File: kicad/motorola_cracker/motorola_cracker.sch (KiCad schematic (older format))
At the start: 27 parts, among them J1 DB9, P1 CONN_6, P2 CONN_2, U1 78L10, U2 74LS245, U3 MAX232, U4 78L05, U5 68HC11_PLCC, X1 4Mhz

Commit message: motorola_cracker update
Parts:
- removed C7: 100n, symbol C
- added P3: CONN_6, symbol CONN_6
- U5: value 68HC11_PLCC -> 68HC05_PLCC
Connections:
- net labels added: TX
- wire segments 98 -> 107
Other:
- moved on the sheet: C2, C3, C9, P1, R2, R7, R8, R9, U5, X1

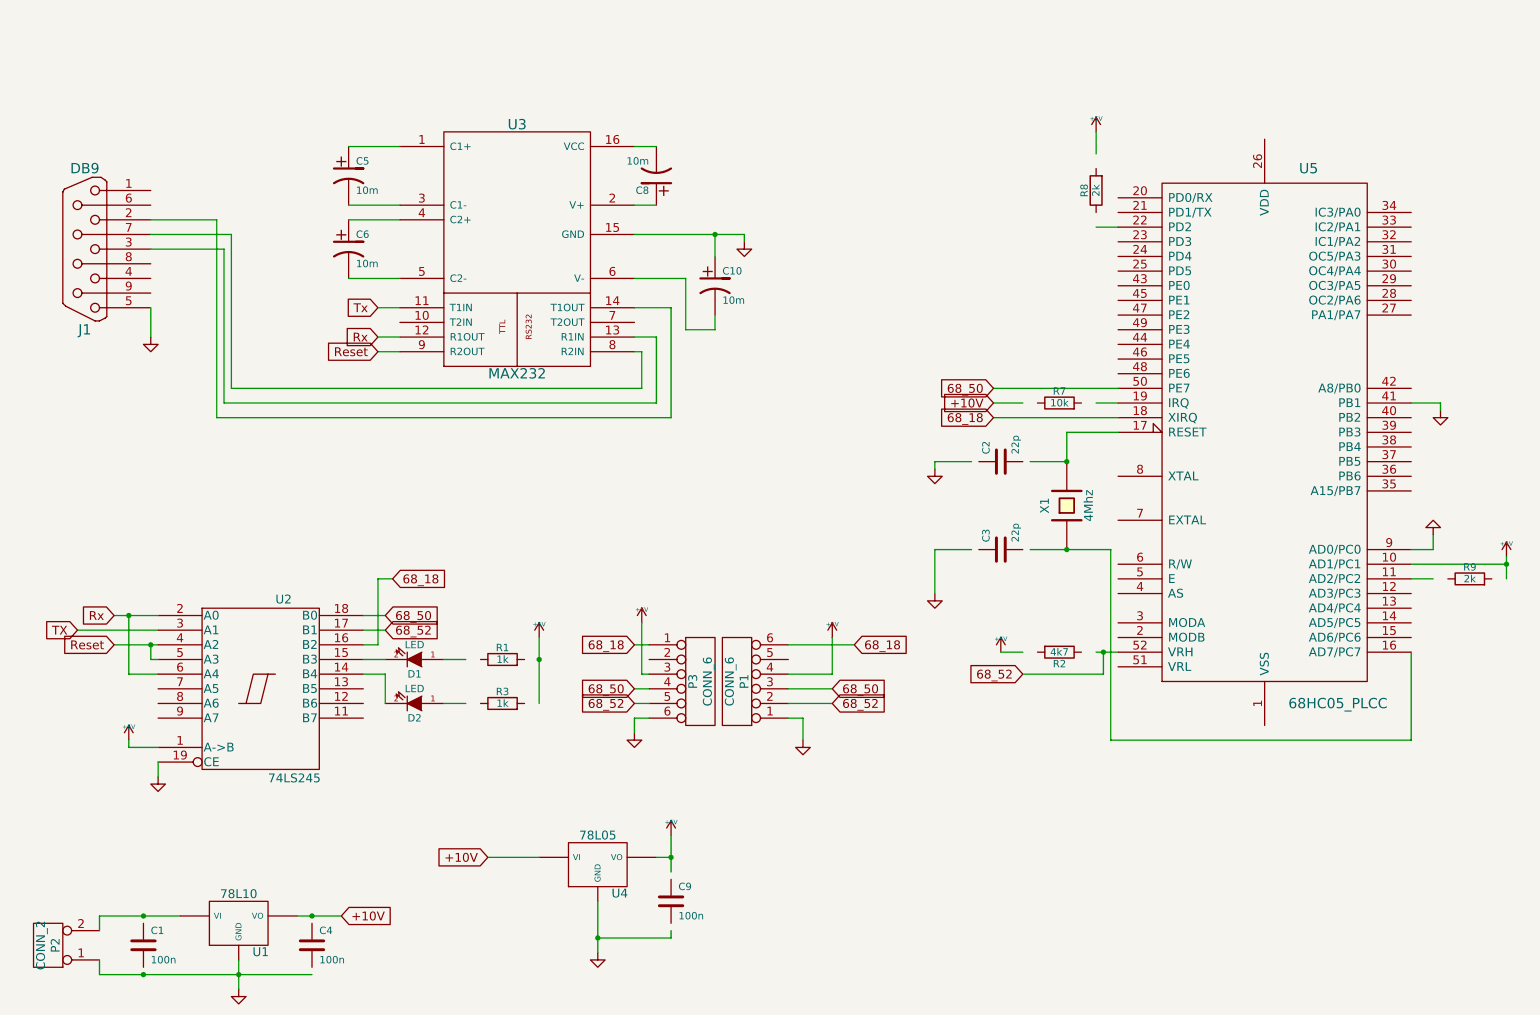
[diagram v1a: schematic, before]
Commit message: update cpu board to fit 50x50cm for dirtypcb servis req.
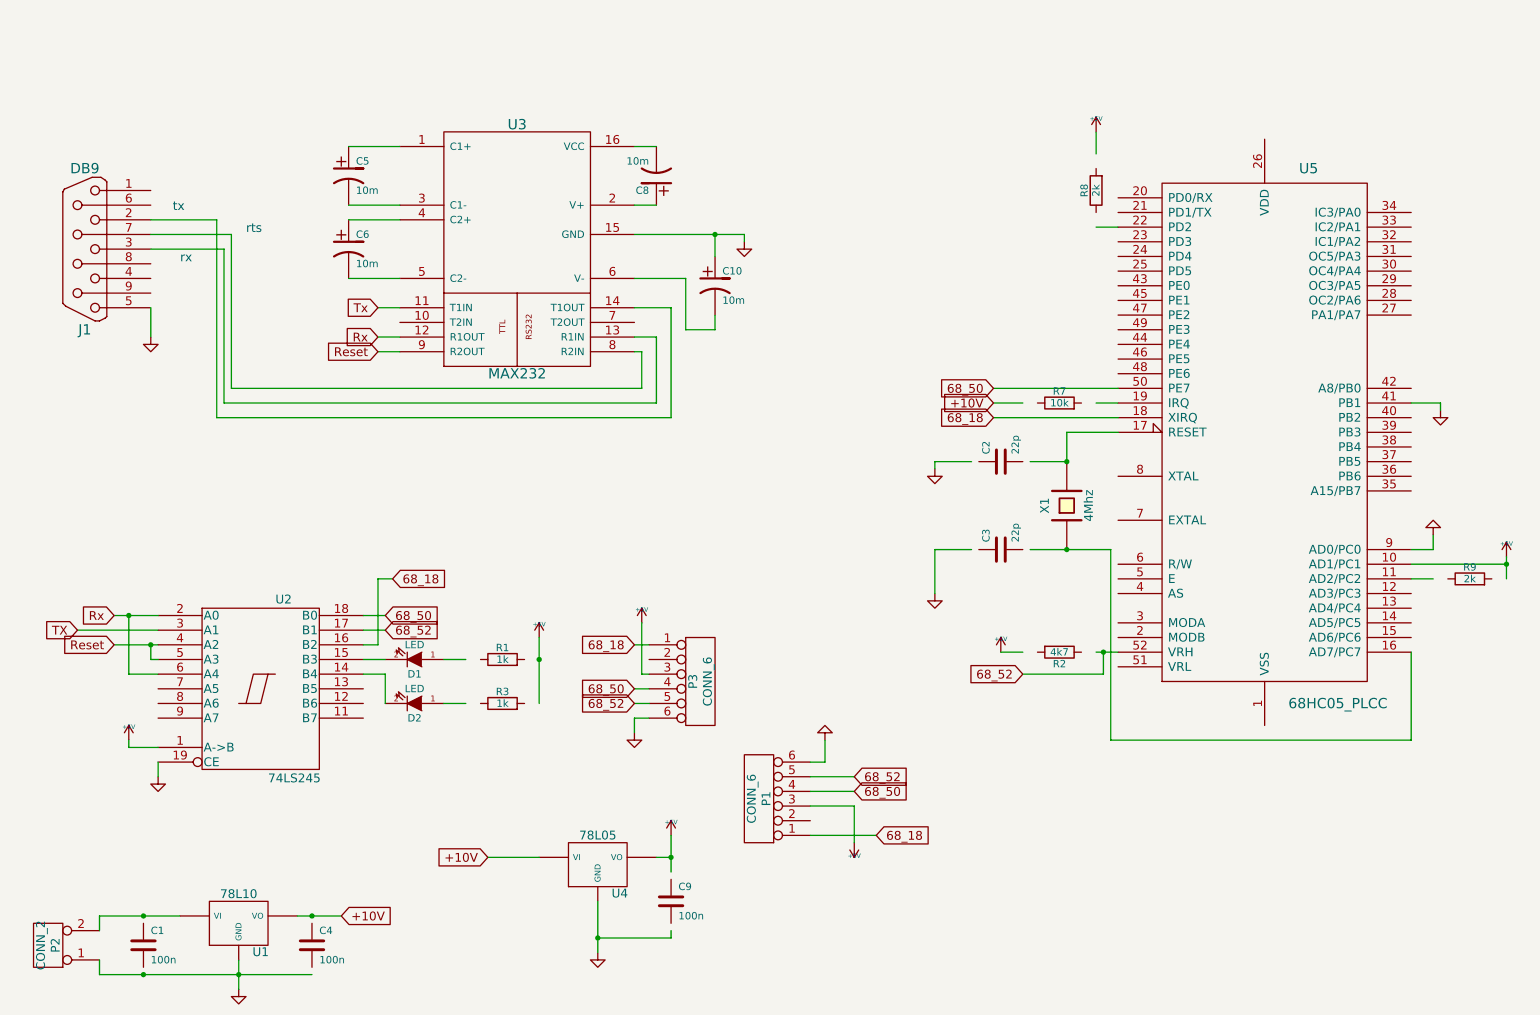
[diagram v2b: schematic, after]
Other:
- note added: "rts"
- note added: "rx"
- note added: "tx"
- moved on the sheet: P1
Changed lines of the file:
@@
 	1    0    0    -1
 $EndComp
-Text GLabel 6200 5550 2    60   Input ~ 0
+Text GLabel 6350 6050 2    60   Input ~ 0
 68_52
-Text GLabel 6350 5150 2    60   Input ~ 0
+Text GLabel 6500 6450 2    60   Input ~ 0
 68_18
-Text GLabel 6200 5450 2    60   Input ~ 0
+Text GLabel 6350 6150 2    60   Input ~ 0
 68_50
 Text GLabel 7500 5350 0    60   Input ~ 0
@@
 L GND #PWR011
 U 1 1 52DBC8C7
-P 6000 5800
-F 0 "#PWR011" H 6000 5800 30  0001 C CNN
-F 1 "GND" H 6000 5730 30  0001 C CNN
-F 2 "" H 6000 5800 60  0001 C CNN
-F 3 "" H 6000 5800 60  0001 C CNN
-	1    6000 5800
-	1    0    0    -1
+P 6150 5800
+F 0 "#PWR011" H 6150 5800 30  0001 C CNN
+F 1 "GND" H 6150 5730 30  0001 C CNN
+F 2 "" H 6150 5800 60  0001 C CNN
+F 3 "" H 6150 5800 60  0001 C CNN
+	1    6150 5800
+	-1   0    0    1
 $EndComp
 $Comp
 L CONN_6 P1
 U 1 1 52DBC7F5
-P 5550 5400
-F 0 "P1" V 5500 5400 60  0000 C CNN
-F 1 "CONN_6" V 5600 5400 60  0000 C CNN
-F 2 "" H 5550 5400 60  0001 C CNN
-F 3 "" H 5550 5400 60  0001 C CNN
-	1    5550 5400
+P 5700 6200
+F 0 "P1" V 5650 6200 60  0000 C CNN
+F 1 "CONN_6" V 5750 6200 60  0000 C CNN
+F 2 "" H 5700 6200 60  0001 C CNN
+F 3 "" H 5700 6200 60  0001 C CNN
+	1    5700 6200
 	-1   0    0    1
 $EndComp
@@
 L +5V #PWR016
 U 1 1 52DAF45F
-P 6200 5100
-F 0 "#PWR016" H 6200 5190 20  0001 C CNN
-F 1 "+5V" H 6200 5190 30  0000 C CNN
-F 2 "" H 6200 5100 60  0001 C CNN
-F 3 "" H 6200 5100 60  0001 C CNN
-	1    6200 5100
-	1    0    0    -1
+P 6350 6500
+F 0 "#PWR016" H 6350 6590 20  0001 C CNN
+F 1 "+5V" H 6350 6590 30  0000 C CNN
+F 2 "" H 6350 6500 60  0001 C CNN
+F 3 "" H 6350 6500 60  0001 C CNN
+	1    6350 6500
+	-1   0    0    1
 $EndComp
 $Comp
@@
 	4850 1750 5000 1750
 Wire Wire Line
-	5900 5150 6350 5150
-Wire Wire Line
-	6200 5550 5900 5550
+	6050 6450 6500 6450
+Wire Wire Line
+	6350 6050 6050 6050
 Wire Wire Line
 	7300 3600 8150 3600
@@
 	1200 7400 1200 7300
 Wire Wire Line
-	6200 5100 6200 5350
-Wire Wire Line
-	6200 5350 5900 5350
+	6350 6250 6350 6500
+Wire Wire Line
+	6350 6250 6050 6250
 Wire Wire Line
 	8000 2300 8150 2300
@@
 	8150 3500 8000 3500
 Wire Wire Line
-	6000 5800 6000 5650
-Wire Wire Line
-	6000 5650 5900 5650
+	6150 5950 6150 5800
+Wire Wire Line
+	6150 5950 6050 5950
 Wire Wire Line
 	1750 7000 1200 7000
@@
 Connection ~ 8050 5200
 Wire Wire Line
-	6200 5450 5900 5450
+	6350 6150 6050 6150
 Wire Wire Line
 	1600 6050 1600 5950
@@
 Wire Wire Line
 	5100 7150 4600 7150
+Text Notes 1700 2200 0    60   ~ 0
+tx
+Text Notes 1750 2550 0    60   ~ 0
+rx
+Text Notes 2200 2350 0    60   ~ 0
+rts
 $EndSCHEMATC

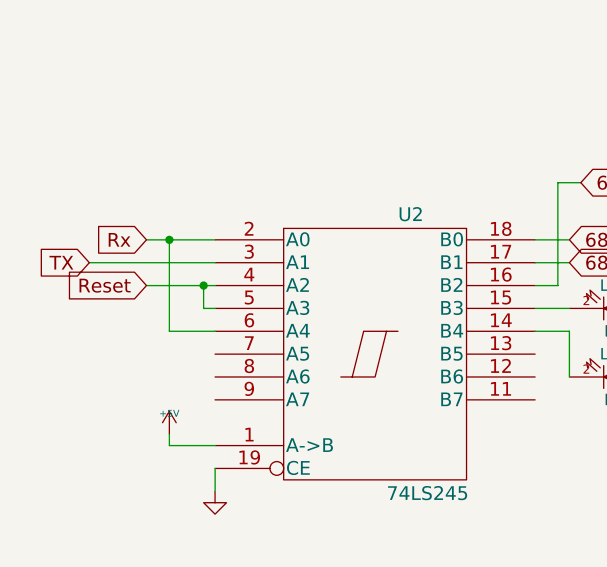
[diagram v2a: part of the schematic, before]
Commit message: remke pcb's to match 5x5cm
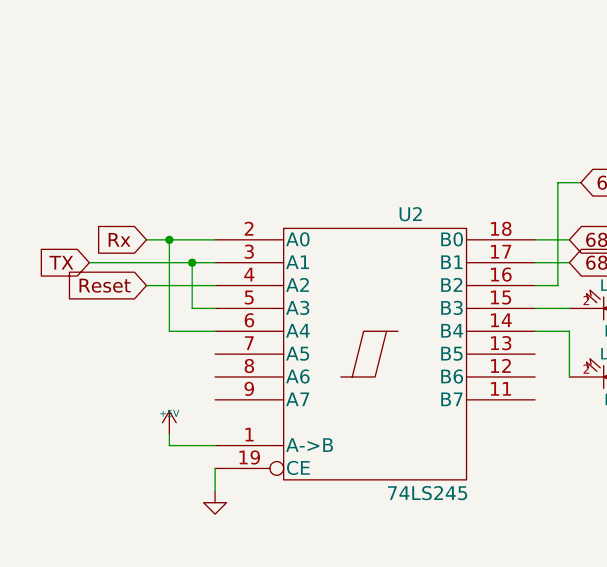
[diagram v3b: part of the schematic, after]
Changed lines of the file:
@@
 Wire Wire Line
 	1300 5150 1600 5150
-Connection ~ 1550 5150
 Wire Wire Line
 	1050 5050 1600 5050
@@
 Connection ~ 4600 7150
 Wire Wire Line
-	1550 5150 1550 5250
-Wire Wire Line
-	1550 5250 1600 5250
+	1500 5250 1600 5250
 Wire Wire Line
 	3250 3050 3100 3050
@@
 Text Notes 2200 2350 0    60   ~ 0
 rts
+Wire Wire Line
+	1500 5250 1500 5050
+Connection ~ 1500 5050
 $EndSCHEMATC

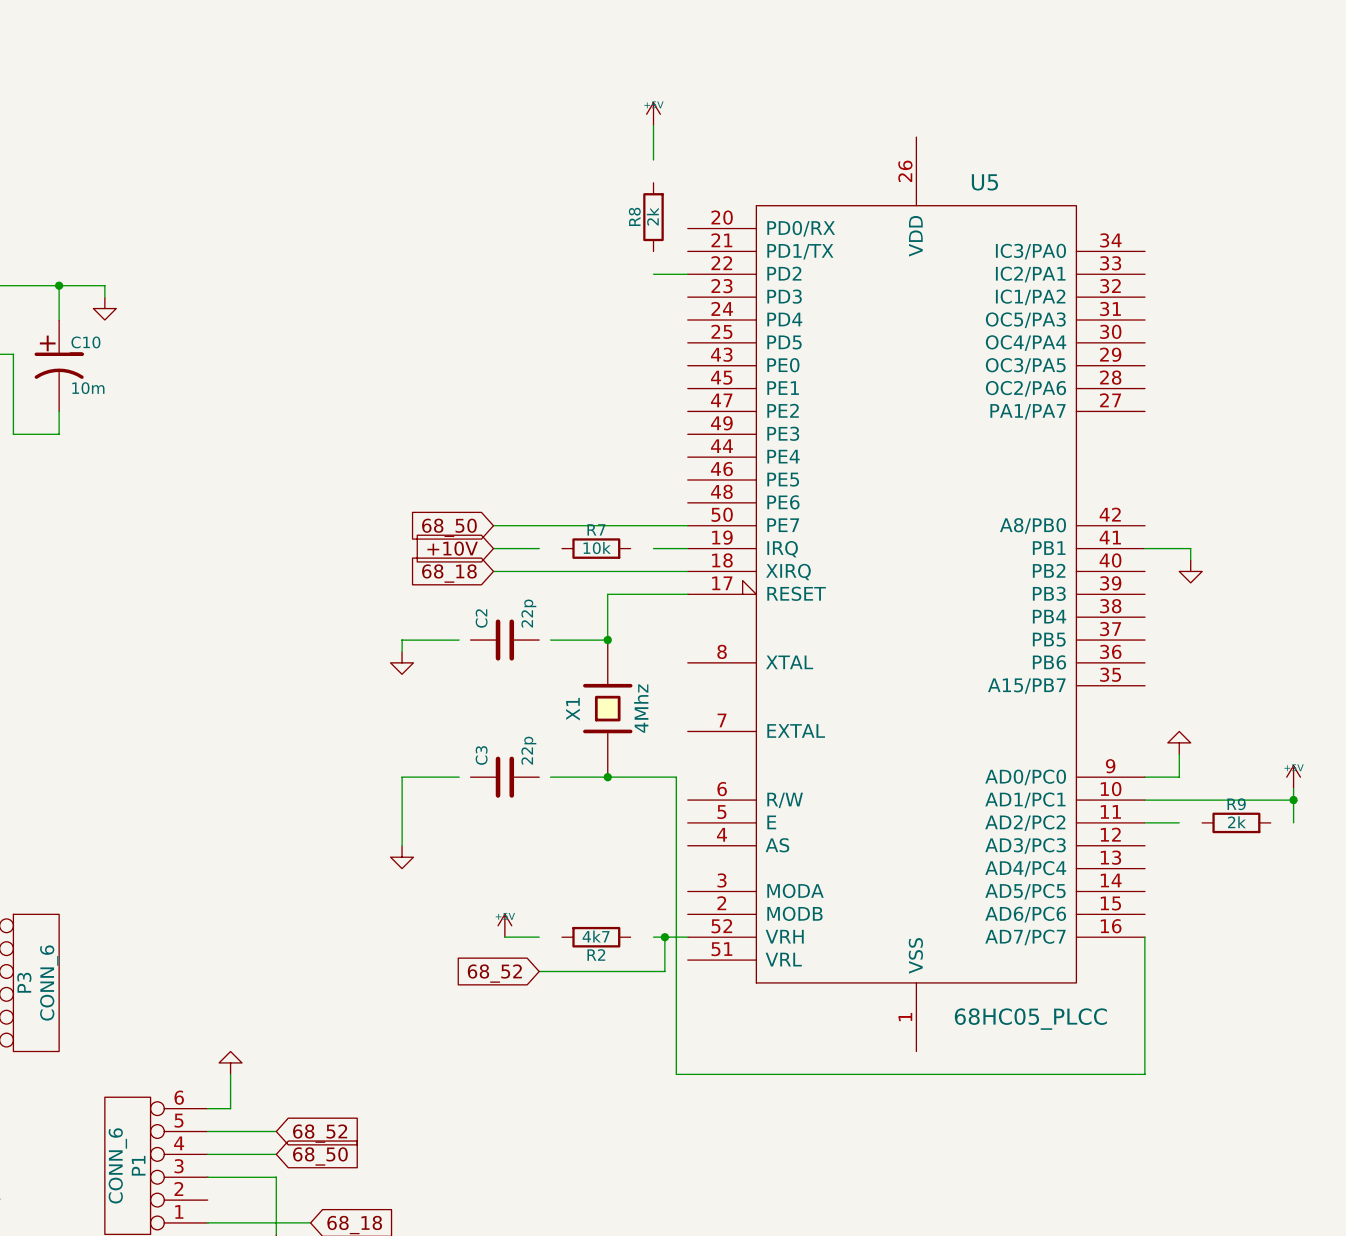
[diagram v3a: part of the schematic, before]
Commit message: added switch to select 68HC05/68HC705 based on schematics mc68hc05-705.JPG
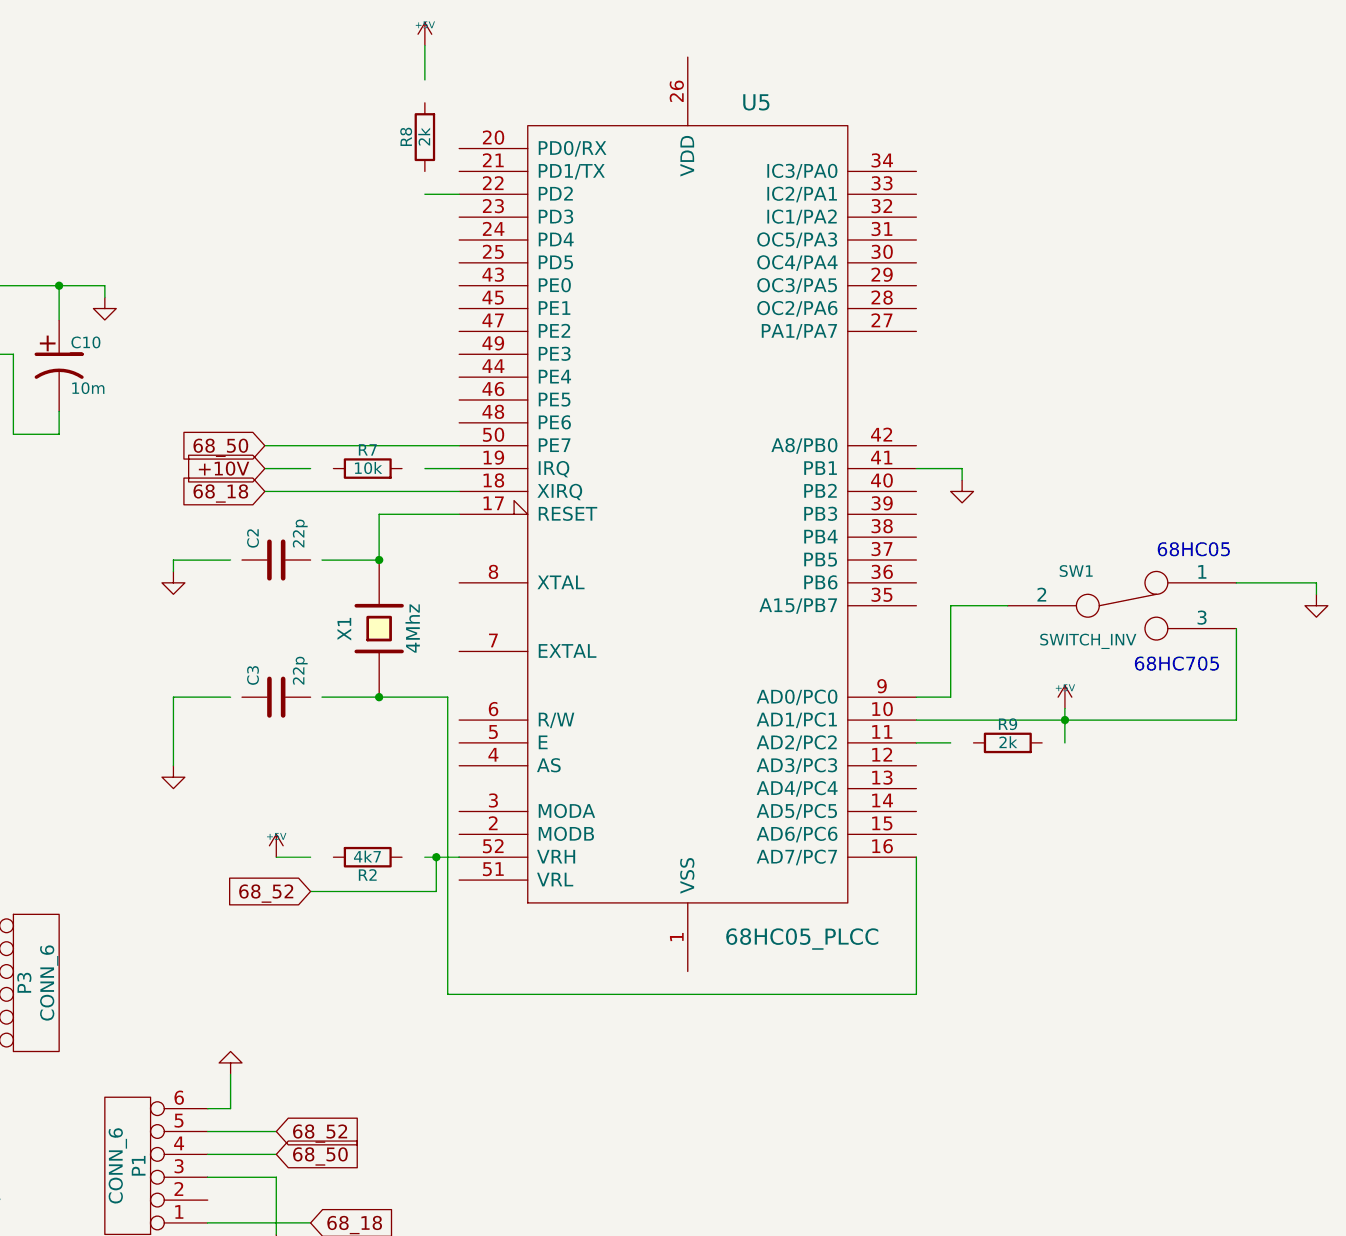
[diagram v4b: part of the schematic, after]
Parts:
- added SW1: SWITCH_INV, Pin_Headers:Pin_Header_Straight_1x03, symbol SWITCH_INV
- C1, C4, C9: footprint (none) -> Capacitors_ThroughHole:Capacitor3MMDiscRM2.5
- C10, C5, C6, C8: footprint (none) -> Capacitors_Elko_ThroughHole:Elko_vert_DM10_RM5
- C2, C3: footprint (none) -> Capacitors_ThroughHole:Capacitor6MMDiscRM5
- D1, D2: footprint (none) -> LEDs:LED-5MM
- J1: footprint (none) -> Connect:DB9FC
- P1: footprint (none) -> Socket_Strips:Socket_Strip_Angled_1x06
- P2: footprint (none) -> Connect:AK300-2
- P3: footprint (none) -> Pin_Headers:Pin_Header_Angled_1x06
- R1, R2, R3, R7, R8, R9: footprint (none) -> Resistors_ThroughHole:Resistor_Horizontal_RM10mm
- U1, U4: footprint (none) -> my_modules:TO92-STABIL
- U2: footprint (none) -> Sockets_DIP:DIP-20__300_ELL
- U3: footprint (none) -> Sockets_DIP:DIP-16__300_ELL
- U5: footprint (none) -> Sockets:PLCC52
- X1: footprint (none) -> Crystals:Crystal_HC49-U_Vertical
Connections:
- wire segments 107 -> 111
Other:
- note added: "68HC05"
- note added: "68HC705"
- moved on the sheet: C2, C3, R2, R7, R8, R9, U5, X1

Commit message: motorola cracker simple board for usb to serial dongle (tested with cp2102)
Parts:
- removed C10, C5, C6, C8: 10m, Capacitors_Elko_ThroughHole:Elko_vert_DM10_RM5, symbol CP1
- removed D1, D2: LED, LEDs:LED-5MM, symbol LED
- removed J1: DB9, Connect:DB9FC, symbol DB9
- removed P3: CONN_6, Pin_Headers:Pin_Header_Angled_1x06, symbol CONN_6
- removed R1, R3: 1k, Resistors_ThroughHole:Resistor_Horizontal_RM10mm, symbol R
- removed R2: 4k7, Resistors_ThroughHole:Resistor_Horizontal_RM10mm, symbol R
- removed SW1: SWITCH_INV, Pin_Headers:Pin_Header_Straight_1x03, symbol SWITCH_INV
- removed U2: 74LS245, Sockets_DIP:DIP-20__300_ELL, symbol 74LS245
- removed U3: MAX232, Sockets_DIP:DIP-16__300_ELL, symbol MAX232
- removed U5: 68HC05_PLCC, Sockets:PLCC52, symbol 68HC11_PLCC
- added C5: 100n, Capacitors_ThroughHole:C_Disc_D3_P2.5, symbol C
- added JP1: JUMPER3, Pin_Headers:Pin_Header_Straight_1x03, symbol JUMPER3
- added P3: CONN_5, Pin_Headers:Pin_Header_Straight_1x01, symbol CONN_01X01
- added R1: 10k, Resistors_ThroughHole:Resistor_Horizontal_RM10mm, symbol R-RESCUE-motorola_cracker
- added R2: 100M, Resistors_ThroughHole:Resistor_Horizontal_RM10mm, symbol R-RESCUE-motorola_cracker
- added U2: 68HC05_PLCC, Sockets:PLCC52, symbol 68HC05_PLCC
- C1, C4: footprint Capacitors_ThroughHole:Capacitor3MMDiscRM2.5 -> Capacitors_ThroughHole:C_Disc_D3_P2.5; symbol C -> C-RESCUE-motorola_cracker
- C2, C3: footprint Capacitors_ThroughHole:Capacitor6MMDiscRM5 -> Capacitors_ThroughHole:C_Rect_L7_W2_P5; symbol C -> C-RESCUE-motorola_cracker
- C9: symbol C -> C-RESCUE-motorola_cracker
- P1: value CONN_6 -> CONN_4; footprint Socket_Strips:Socket_Strip_Angled_1x06 -> Pin_Headers:Pin_Header_Straight_1x04; symbol CONN_6 -> CONN_01X04
- P2: value CONN_2 -> CONN_1; symbol CONN_2 -> CONN_01X02
- R7: symbol R -> R-RESCUE-motorola_cracker
- R8, R9: value 2k -> 1k; symbol R -> R-RESCUE-motorola_cracker
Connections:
- net labels added: RESET, RX
- net labels removed: 68_18, 68_50, 68_52, Reset, Rx, Tx
- wire segments 111 -> 52
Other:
- note removed: "rts"
- note removed: "rx"
- note removed: "tx"
- moved on the sheet: C1, C2, C3, C4, C9, P2, R7, R8, R9, U1, U4, X1

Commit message: simplified version
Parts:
- removed C1, C4: 100n, Capacitors_ThroughHole:C_Disc_D3_P2.5, symbol C-RESCUE-motorola_cracker
- removed C5: 100n, Capacitors_ThroughHole:C_Disc_D3_P2.5, symbol C
- removed C9: 100n, Capacitors_ThroughHole:Capacitor3MMDiscRM2.5, symbol C-RESCUE-motorola_cracker
- removed U1: 78L10, my_modules:TO92-STABIL, symbol 78L05
- removed U4: 78L05, my_modules:TO92-STABIL, symbol 78L05
- C2, C3: footprint Capacitors_ThroughHole:C_Rect_L7_W2_P5 -> Capacitors_SMD:C_1206; symbol C-RESCUE-motorola_cracker -> C
- P1: value CONN_4 -> UART
- P2: value CONN_1 -> +12V; footprint Connect:AK300-2 -> Socket_Strips:Socket_Strip_Straight_1x02
- P3: value CONN_5 -> RTS
- R1, R2, R7, R8, R9: footprint Resistors_ThroughHole:Resistor_Horizontal_RM10mm -> Resistors_SMD:R_1206; symbol R-RESCUE-motorola_cracker -> R
- X1: symbol CRYSTAL -> Crystal
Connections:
- net +10V is gone; now on net +12V: R7.1
- net +12V: now reaches P2.2 (P2)
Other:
- moved on the sheet: C2, C3, R2
